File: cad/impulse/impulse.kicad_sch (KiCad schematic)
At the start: 18 parts, among them J1 Conn_02x04_Counter_Clockwise, U1 STM32G431CBUx, Y1 X252016MLB4SI

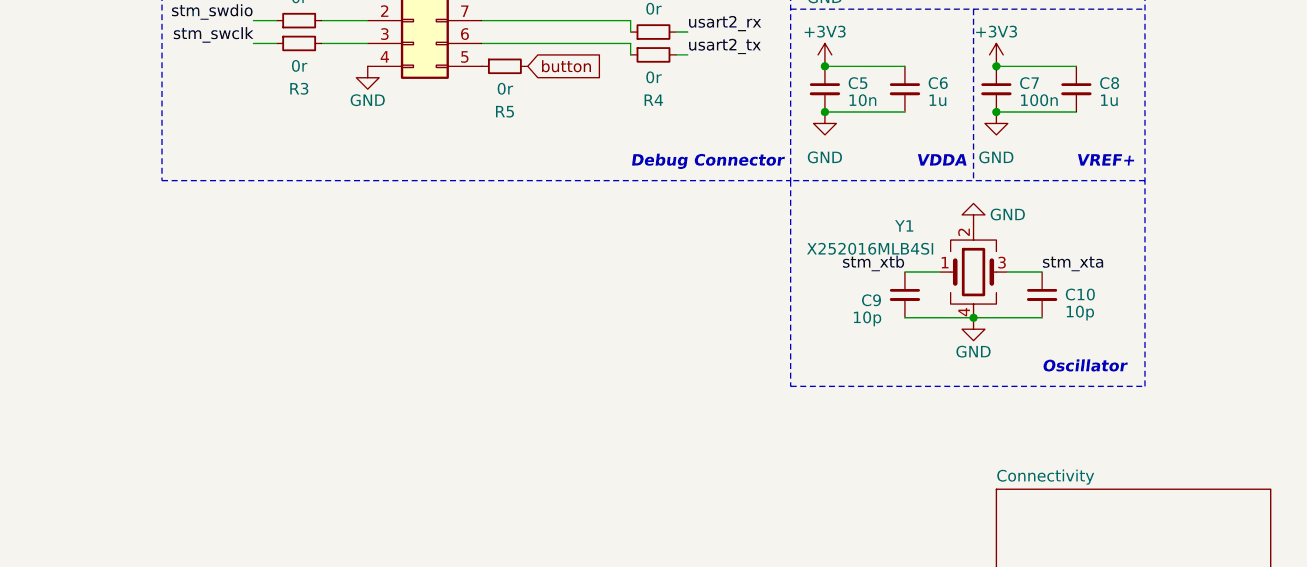
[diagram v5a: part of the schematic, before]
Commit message: Modified oscillator circuit.
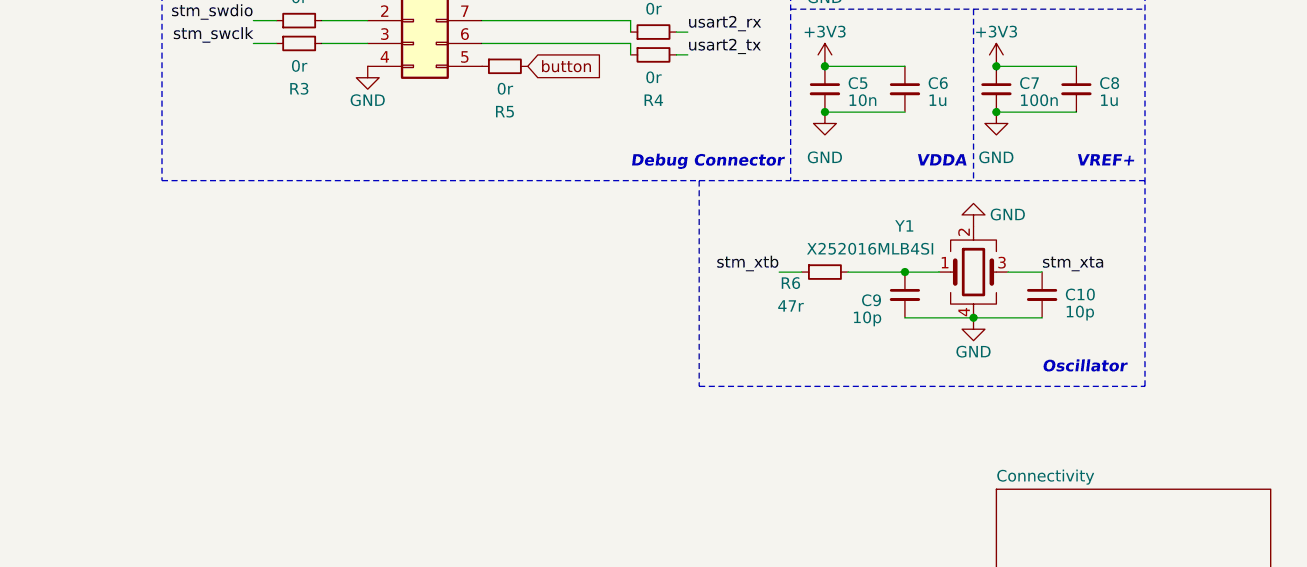
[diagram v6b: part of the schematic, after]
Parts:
- added R6: 47r, Resistor_SMD:R_0402_1005Metric, symbol Device:R_Small
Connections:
- net stm_xtb: now also R6.1; no longer C9.1, Y1.1
- new net: C9.1, R6.2, Y1.1
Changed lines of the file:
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@@
   (junction (at 248.92 29.21) (diameter 0) (color 0 0 0 0)
   )
+  (junction (at 240.03 64.77) (diameter 0) (color 0 0 0 0)
+  )
   (junction (at 231.14 29.21) (diameter 0) (color 0 0 0 0)
   )
@@
     (stroke (width 0) (type dash))
   )
+  (wire (pts (xy 226.06 64.77) (xy 228.6 64.77))
+    (stroke (width 0) (type default))
+  )
   (wire (pts (xy 231.14 41.91) (xy 240.03 41.91))
     (stroke (width 0) (type default))
@@
     (stroke (width 0) (type default))
   )
+  (wire (pts (xy 233.68 64.77) (xy 240.03 64.77))
+    (stroke (width 0) (type default))
+  )
   (wire (pts (xy 175.26 36.83) (xy 180.34 36.83))
     (stroke (width 0) (type default))
@@
     (stroke (width 0) (type default))
   )
-  (polyline (pts (xy 227.33 77.47) (xy 266.7 77.47))
+  (polyline (pts (xy 217.17 77.47) (xy 266.7 77.47))
     (stroke (width 0) (type dash))
   )
@@
     (stroke (width 0) (type default))
   )
+  (wire (pts (xy 95.25 43.18) (xy 97.79 43.18))
+    (stroke (width 0) (type default))
+  )
+  (wire (pts (xy 97.79 39.37) (xy 97.79 43.18))
+    (stroke (width 0) (type default))
+  )
+  (wire (pts (xy 97.79 43.18) (xy 100.33 43.18))
+    (stroke (width 0) (type default))
+  )
+  (wire (pts (xy 100.33 43.18) (xy 102.87 43.18))
+    (stroke (width 0) (type default))
+  )
+  (wire (pts (xy 167.64 36.83) (xy 170.18 36.83))
+    (stroke (width 0) (type default))
+  )
+  (wire (pts (xy 66.04 96.52) (xy 80.01 96.52))
+    (stroke (width 0) (type default))
+  )
+  (wire (pts (xy 240.03 29.21) (xy 248.92 29.21))
+    (stroke (width 0) (type default))
+  )
+  (polyline (pts (xy 157.48 54.61) (xy 217.17 54.61))
+    (stroke (width 0) (type dash))
+  )
+  (wire (pts (xy 193.04 39.37) (xy 209.55 39.37))
+    (stroke (width 0) (type default))
+  )
+  (polyline (pts (xy 266.7 77.47) (xy 266.7 54.61))
+    (stroke (width 0) (type dash))
+  )
+  (polyline (pts (xy 266.7 19.05) (xy 266.7 54.61))
+    (stroke (width 0) (type dash))
+  )
+  (wire (pts (xy 240.03 24.13) (xy 248.92 24.13))
+    (stroke (width 0) (type default))
+  )
+  (wire (pts (xy 113.03 76.2) (xy 123.19 76.2))
+    (stroke (width 0) (type default))
+  )
+  (wire (pts (xy 240.03 69.85) (xy 247.65 69.85))
+    (stroke (width 0) (type default))
+  )
+  (polyline (pts (xy 217.17 54.61) (xy 217.17 77.47))
+    (stroke (width 0) (type dash))
+  )
+  (wire (pts (xy 231.14 24.13) (xy 240.03 24.13))
+    (stroke (width 0) (type default))
+  )
+  (wire (pts (xy 214.63 38.1) (xy 215.9 38.1))
+    (stroke (width 0) (type default))
+  )
+  (polyline (pts (xy 266.7 54.61) (xy 227.33 54.61))
+    (stroke (width 0) (type dash))
+  )
+  (wire (pts (xy 231.14 46.99) (xy 240.03 46.99))
+    (stroke (width 0) (type default))
+  )
   (wire (pts (xy 240.03 64.77) (xy 243.84 64.77))
     (stroke (width 0) (type default))
   )
-  (wire (pts (xy 95.25 43.18) (xy 97.79 43.18))
-    (stroke (width 0) (type default))
-  )
-  (wire (pts (xy 97.79 39.37) (xy 97.79 43.18))
-    (stroke (width 0) (type default))
-  )
-  (wire (pts (xy 97.79 43.18) (xy 100.33 43.18))
-    (stroke (width 0) (type default))
-  )
-  (wire (pts (xy 100.33 43.18) (xy 102.87 43.18))
-    (stroke (width 0) (type default))
-  )
-  (wire (pts (xy 167.64 36.83) (xy 170.18 36.83))
-    (stroke (width 0) (type default))
-  )
-  (wire (pts (xy 66.04 96.52) (xy 80.01 96.52))
-    (stroke (width 0) (type default))
-  )
-  (wire (pts (xy 240.03 29.21) (xy 248.92 29.21))
-    (stroke (width 0) (type default))
-  )
-  (polyline (pts (xy 157.48 54.61) (xy 227.33 54.61))
-    (stroke (width 0) (type dash))
-  )
-  (wire (pts (xy 193.04 39.37) (xy 209.55 39.37))
-    (stroke (width 0) (type default))
-  )
-  (polyline (pts (xy 266.7 77.47) (xy 266.7 54.61))
-    (stroke (width 0) (type dash))
-  )
-  (polyline (pts (xy 266.7 19.05) (xy 266.7 54.61))
-    (stroke (width 0) (type dash))
-  )
-  (wire (pts (xy 240.03 24.13) (xy 248.92 24.13))
-    (stroke (width 0) (type default))
-  )
-  (wire (pts (xy 113.03 76.2) (xy 123.19 76.2))
-    (stroke (width 0) (type default))
-  )
-  (wire (pts (xy 240.03 69.85) (xy 247.65 69.85))
-    (stroke (width 0) (type default))
-  )
-  (polyline (pts (xy 227.33 54.61) (xy 227.33 77.47))
-    (stroke (width 0) (type dash))
-  )
-  (wire (pts (xy 231.14 24.13) (xy 240.03 24.13))
-    (stroke (width 0) (type default))
-  )
-  (wire (pts (xy 214.63 38.1) (xy 215.9 38.1))
-    (stroke (width 0) (type default))
-  )
-  (polyline (pts (xy 266.7 54.61) (xy 227.33 54.61))
-    (stroke (width 0) (type dash))
-  )
-  (wire (pts (xy 231.14 46.99) (xy 240.03 46.99))
-    (stroke (width 0) (type default))
-  )
   (wire (pts (xy 248.92 29.21) (xy 257.81 29.21))
     (stroke (width 0) (type default))
@@
   )
   (polyline (pts (xy 247.65 35.56) (xy 247.65 54.61))
+    (stroke (width 0) (type dash))
+  )
+  (polyline (pts (xy 217.17 54.61) (xy 227.33 54.61))
     (stroke (width 0) (type dash))
   )
@@
     (effects (font (size 1.27 1.27)) (justify left bottom))
   )
-  (label "stm_xtb" (at 240.03 64.77 180) (fields_autoplaced)
+  (label "stm_xtb" (at 226.06 64.77 180) (fields_autoplaced)
     (effects (font (size 1.27 1.27)) (justify right bottom))
   )
@@
         )
       )
+    )
+  )
+  (symbol (lib_id "Device:R_Small") (at 231.14 64.77 90) (mirror x) (unit 1)
+    (in_bom yes) (on_board yes) (dnp no)
+    (property "Reference" "R6" (at 227.33 66.04 90)
+      (effects (font (size 1.27 1.27)))
+    )
+    (property "Value" "47r" (at 227.33 68.58 90)
+      (effects (font (size 1.27 1.27)))
+    )
+    (property "Footprint" "Resistor_SMD:R_0402_1005Metric" (at 231.14 64.77 0)
+      (effects (font (size 1.27 1.27)) hide)
+    )
+    (property "Datasheet" "~" (at 231.14 64.77 0)
+      (effects (font (size 1.27 1.27)) hide)
+    )
+    (pin "1")
+    (pin "2")
+    (instances
+      (project "impulse"
+        (path "/eb4cfece-5fcb-437a-ac58-337ab6512039"
+          (reference "R6") (unit 1)
+        )
+      )

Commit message: First layout.
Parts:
- removed R1, R2, R3, R4: 0r, Resistor_SMD:R_0402_1005Metric, symbol Device:R_Small
- J1: footprint Connector_PinHeader_1.27mm:PinHeader_2x04_P1.27mm_Vertical -> Connector_PinHeader_1.27mm:PinHeader_2x04_P1.27mm_Vertical_SMD
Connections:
- net stm_swclk: now also J1.3 (Pin_3)
- net stm_swdio: now also J1.2 (Pin_2)
- net usart2_rx: now also J1.7 (Pin_7)
- net usart2_tx: now also J1.6 (Pin_6)
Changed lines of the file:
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@@
   (junction (at 97.79 43.18) (diameter 0) (color 0 0 0 0)
   )
-  (wire (pts (xy 175.26 39.37) (xy 180.34 39.37))
-    (stroke (width 0) (type default))
-  )
   (wire (pts (xy 66.04 93.98) (xy 80.01 93.98))
     (stroke (width 0) (type default))
@@
     (stroke (width 0) (type default))
   )
-  (wire (pts (xy 167.64 39.37) (xy 170.18 39.37))
+  (wire (pts (xy 177.8 39.37) (xy 180.34 39.37))
     (stroke (width 0) (type default))
   )
@@
     (stroke (width 0) (type default))
   )
-  (wire (pts (xy 209.55 39.37) (xy 209.55 40.64))
-    (stroke (width 0) (type default))
-  )
   (polyline (pts (xy 227.33 19.05) (xy 266.7 19.05))
     (stroke (width 0) (type dash))
@@
     (stroke (width 0) (type default))
   )
-  (wire (pts (xy 193.04 36.83) (xy 209.55 36.83))
-    (stroke (width 0) (type default))
-  )
-  (wire (pts (xy 214.63 40.64) (xy 215.9 40.64))
+  (wire (pts (xy 193.04 36.83) (xy 195.58 36.83))
     (stroke (width 0) (type default))
   )
@@
     (stroke (width 0) (type default))
   )
-  (wire (pts (xy 175.26 36.83) (xy 180.34 36.83))
+  (wire (pts (xy 177.8 36.83) (xy 180.34 36.83))
     (stroke (width 0) (type default))
   )
@@
     (stroke (width 0) (type default))
   )
-  (wire (pts (xy 167.64 36.83) (xy 170.18 36.83))
-    (stroke (width 0) (type default))
-  )
   (wire (pts (xy 66.04 96.52) (xy 80.01 96.52))
     (stroke (width 0) (type default))
@@
     (stroke (width 0) (type dash))
   )
-  (wire (pts (xy 193.04 39.37) (xy 209.55 39.37))
+  (wire (pts (xy 193.04 39.37) (xy 195.58 39.37))
     (stroke (width 0) (type default))
   )
@@
     (stroke (width 0) (type default))
   )
-  (wire (pts (xy 214.63 38.1) (xy 215.9 38.1))
-    (stroke (width 0) (type default))
-  )
   (polyline (pts (xy 266.7 54.61) (xy 227.33 54.61))
     (stroke (width 0) (type dash))
@@
   (polyline (pts (xy 217.17 54.61) (xy 227.33 54.61))
     (stroke (width 0) (type dash))
-  )
-  (wire (pts (xy 209.55 36.83) (xy 209.55 38.1))
-    (stroke (width 0) (type default))
   )
   (text "VREF+" (at 259.08 53.34 0)
@@
     (effects (font (size 1.27 1.27) (thickness 0.254) bold italic) (justify left bottom))
   )
-  (label "usart2_rx" (at 215.9 38.1 0) (fields_autoplaced)
+  (label "usart2_rx" (at 195.58 36.83 0) (fields_autoplaced)
     (effects (font (size 1.27 1.27)) (justify left bottom))
   )
@@
     (effects (font (size 1.27 1.27)) (justify left bottom))
   )
-  (label "stm_swdio" (at 167.64 36.83 180) (fields_autoplaced)
+  (label "stm_swdio" (at 177.8 36.83 180) (fields_autoplaced)
     (effects (font (size 1.27 1.27)) (justify right bottom))
   )
@@
     (effects (font (size 1.27 1.27)) (justify right bottom))
   )
-  (label "usart2_tx" (at 215.9 40.64 0) (fields_autoplaced)
+  (label "usart2_tx" (at 195.58 39.37 0) (fields_autoplaced)
     (effects (font (size 1.27 1.27)) (justify left bottom))
   )
@@
     (effects (font (size 1.27 1.27)) (justify left bottom))
   )
-  (label "stm_swclk" (at 167.64 39.37 180) (fields_autoplaced)
+  (label "stm_swclk" (at 177.8 39.37 180) (fields_autoplaced)
     (effects (font (size 1.27 1.27)) (justify right bottom))
   )
@@
       (effects (font (size 1.27 1.27)))
     )
-    (property "Footprint" "Connector_PinHeader_1.27mm:PinHeader_2x04_P1.27mm_Vertical" (at 185.42 36.83 0)
+    (property "Footprint" "Connector_PinHeader_1.27mm:PinHeader_2x04_P1.27mm_Vertical_SMD" (at 185.42 36.83 0)
       (effects (font (size 1.27 1.27)) hide)
     )
@@
     )
   )
-  (symbol (lib_id "Device:R_Small") (at 172.72 36.83 90) (unit 1)
-    (in_bom yes) (on_board yes) (dnp no)
-    (property "Reference" "R1" (at 172.72 31.75 90)
-      (effects (font (size 1.27 1.27)))
-    )
-    (property "Value" "0r" (at 172.72 34.29 90)
-      (effects (font (size 1.27 1.27)))
-    )
-    (property "Footprint" "Resistor_SMD:R_0402_1005Metric" (at 172.72 36.83 0)
-      (effects (font (size 1.27 1.27)) hide)
-    )
-    (property "Datasheet" "~" (at 172.72 36.83 0)
-      (effects (font (size 1.27 1.27)) hide)
-    )
-    (property "lcsc" "C21376" (at 172.72 36.83 0)
-      (effects (font (size 1.27 1.27)) hide)
-    )
-    (pin "1")
-    (pin "2")
-    (instances
-      (project "impulse"
-        (path "/eb4cfece-5fcb-437a-ac58-337ab6512039"
-          (reference "R1") (unit 1)
-        )
-      )
-    )
-  )
-  (symbol (lib_id "Device:R_Small") (at 172.72 39.37 90) (mirror x) (unit 1)
-    (in_bom yes) (on_board yes) (dnp no)
-    (property "Reference" "R3" (at 172.72 44.45 90)
-      (effects (font (size 1.27 1.27)))
-    )
-    (property "Value" "0r" (at 172.72 41.91 90)
-      (effects (font (size 1.27 1.27)))
-    )
-    (property "Footprint" "Resistor_SMD:R_0402_1005Metric" (at 172.72 39.37 0)
-      (effects (font (size 1.27 1.27)) hide)
-    )
-    (property "Datasheet" "~" (at 172.72 39.37 0)
-      (effects (font (size 1.27 1.27)) hide)
-    )
-    (property "lcsc" "C21376" (at 172.72 39.37 0)
-      (effects (font (size 1.27 1.27)) hide)
-    )
-    (pin "1")
-    (pin "2")
-    (instances
-      (project "impulse"
-        (path "/eb4cfece-5fcb-437a-ac58-337ab6512039"
-          (reference "R3") (unit 1)
-        )
-      )
-    )
-  )
-  (symbol (lib_id "Device:R_Small") (at 212.09 40.64 90) (mirror x) (unit 1)
-    (in_bom yes) (on_board yes) (dnp no)
-    (property "Reference" "R4" (at 212.09 45.72 90)
-      (effects (font (size 1.27 1.27)))
-    )
-    (property "Value" "0r" (at 212.09 43.18 90)
-      (effects (font (size 1.27 1.27)))
-    )
-    (property "Footprint" "Resistor_SMD:R_0402_1005Metric" (at 212.09 40.64 0)
-      (effects (font (size 1.27 1.27)) hide)
-    )
-    (property "Datasheet" "~" (at 212.09 40.64 0)
-      (effects (font (size 1.27 1.27)) hide)
-    )
-    (property "lcsc" "C21376" (at 212.09 40.64 0)
-      (effects (font (size 1.27 1.27)) hide)
-    )
-    (pin "1")
-    (pin "2")
-    (instances
-      (project "impulse"
-        (path "/eb4cfece-5fcb-437a-ac58-337ab6512039"
-          (reference "R4") (unit 1)
-        )
-      )
-    )
-  )
   (symbol (lib_id "Device:R_Small") (at 195.58 41.91 90) (mirror x) (unit 1)
     (in_bom yes) (on_board yes) (dnp no)
@@
         )
       )
-    )
-  )
-  (symbol (lib_id "Device:R_Small") (at 212.09 38.1 90) (unit 1)
-    (in_bom yes) (on_board yes) (dnp no)
-    (property "Reference" "R2" (at 212.09 33.02 90)
-      (effects (font (size 1.27 1.27)))
-    )
-    (property "Value" "0r" (at 212.09 35.56 90)
-      (effects (font (size 1.27 1.27)))
-    )
-    (property "Footprint" "Resistor_SMD:R_0402_1005Metric" (at 212.09 38.1 0)
-      (effects (font (size 1.27 1.27)) hide)
-    )
-    (property "Datasheet" "~" (at 212.09 38.1 0)
-      (effects (font (size 1.27 1.27)) hide)
-    )
-    (property "lcsc" "C21376" (at 212.09 38.1 0)
-      (effects (font (size 1.27 1.27)) hide)
-    )
-    (pin "1")
-    (pin "2")
-    (instances
-      (project "impulse"
-        (path "/eb4cfece-5fcb-437a-ac58-337ab6512039"
-          (reference "R2") (unit 1)
-        )
-      )

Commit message: Final version, ordered it.
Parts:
- R6: lcsc (none) -> C2906947
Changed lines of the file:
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@@
+      (effects (font (size 1.27 1.27)) hide)
+    )
+    (property "lcsc" "C2906947" (at 231.14 64.77 0)
       (effects (font (size 1.27 1.27)) hide)
     )
